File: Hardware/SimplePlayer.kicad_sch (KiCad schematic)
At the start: 4 parts, among them U1 CS43198, U2 XIAO-ESP32S3, U3 OPA1622, U4 OPA1622

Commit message: Schematic sheets
Added new schematic sheets for each system.
Missing some microcontroller connections.
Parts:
- removed U1: CS43198, Custom_Parts:VQFN-40-1EP_5x5mm_P0.4mm_EP3.5x3.5mm_ThermalVias, symbol Custom_Parts:CS43198
- removed U2: XIAO-ESP32S3, Custom_Parts:XIAO-ESP32S3-SMD, symbol Custom_Parts:XIAO-ESP32S3-SMD
- removed U3, U4: OPA1622, Package_SON:Texas_S-PVSON-N10, symbol Amplifier_Audio:OPA1622
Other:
- added sheet Audio (Audio.kicad_sch)
- added sheet Microcontoller (Microcontroller.kicad_sch)
- added sheet Power (Power.kicad_sch)

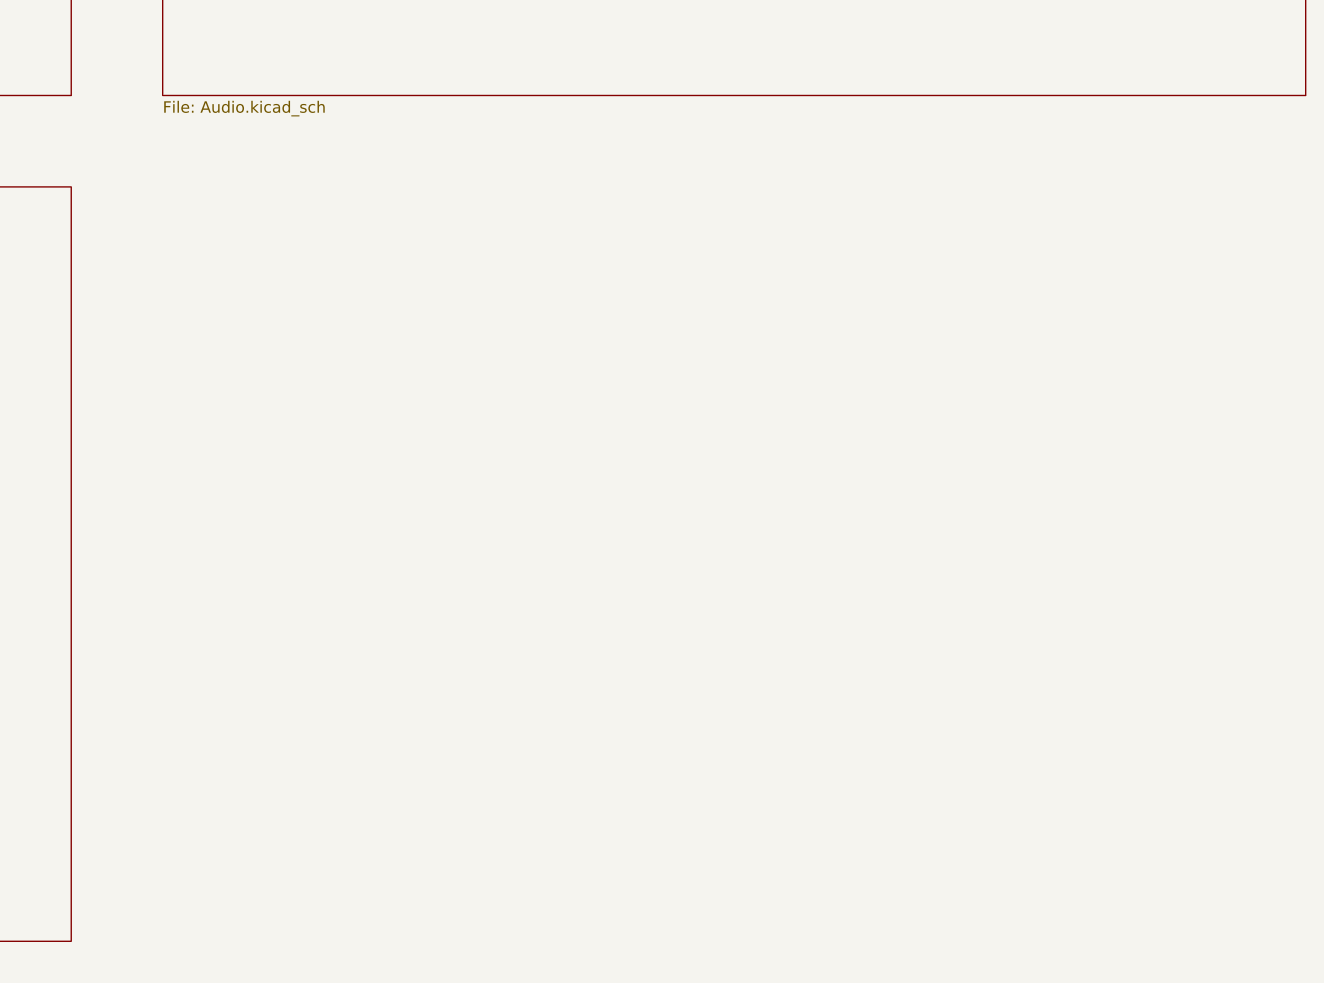
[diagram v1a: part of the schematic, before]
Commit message: Expander and IO
Added an IO expander to the design.
Finished the main connections between the basic components.
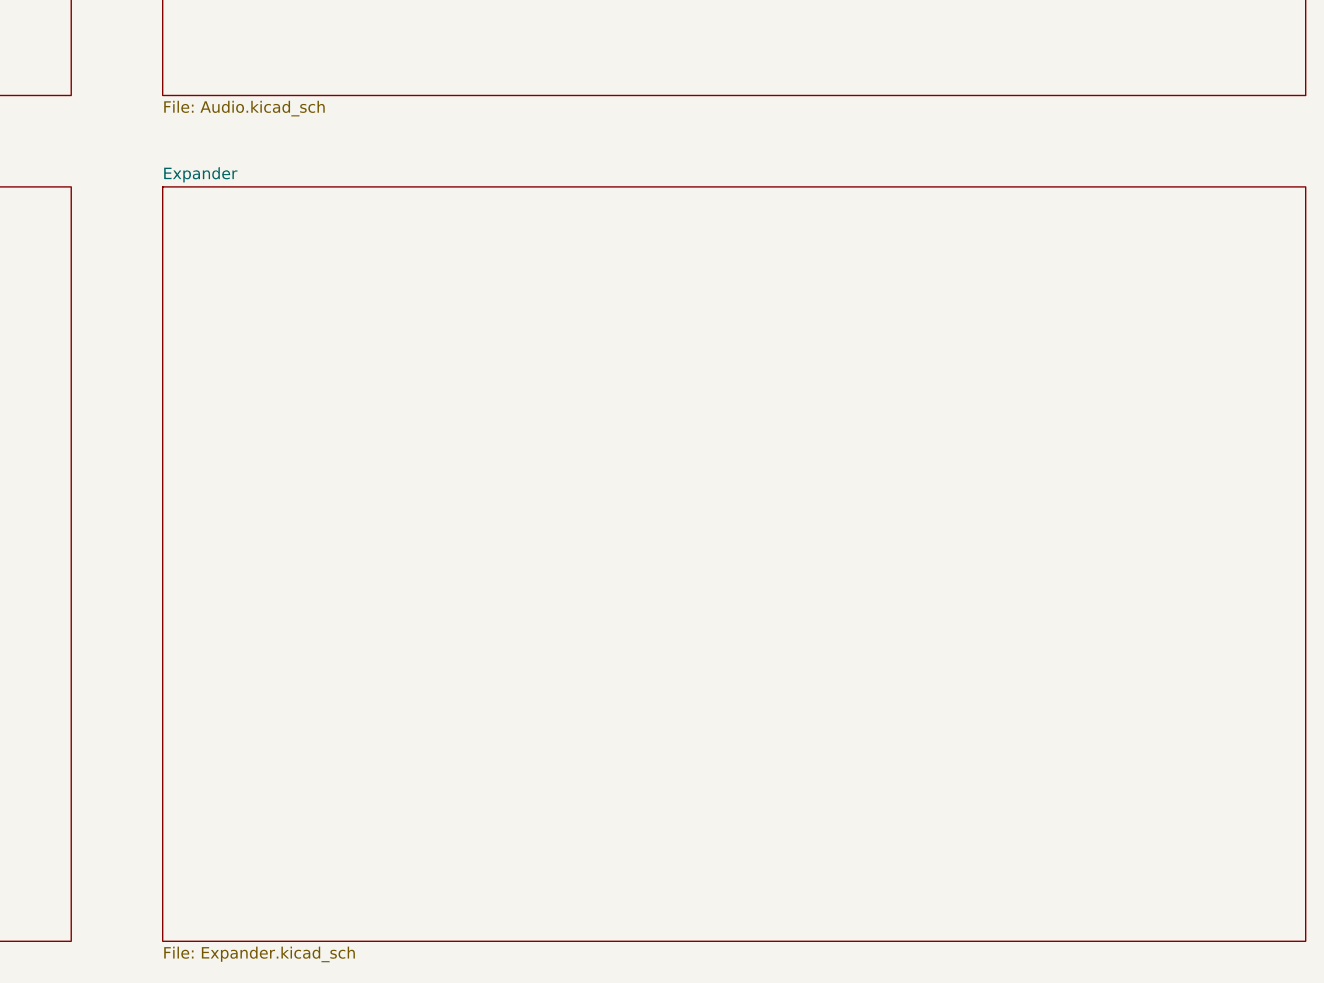
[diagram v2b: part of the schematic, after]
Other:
- added sheet Expander (Expander.kicad_sch)
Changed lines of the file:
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@@
+		)
+	)
+	(sheet
+		(at 210.82 152.4)
+		(size 127 83.82)
+		(exclude_from_sim no)
+		(in_bom yes)
+		(on_board yes)
+		(dnp no)
+		(fields_autoplaced yes)
+		(stroke
+			(width 0.1524)
+			(type solid)
+		)
+		(fill
+			(color 0 0 0 0)
+		)
+		(property "Sheetname" "Expander"
+			(at 210.82 151.6884 0)
+			(show_name no)
+			(do_not_autoplace no)
+			(effects
+				(font
+					(size 1.27 1.27)
+				)
+				(justify left bottom)
+			)
+		)
+		(property "Sheetfile" "Expander.kicad_sch"
+			(at 210.82 236.8046 0)
+			(show_name no)
+			(do_not_autoplace no)
+			(effects
+				(font
+					(size 1.27 1.27)
+				)
+				(justify left top)
+			)
+		)
+		(instances
+			(project "SimplePlayer"
+				(path "/361b87fa-3e7e-4f22-890f-5dc32caef103"
+					(page "5")
+				)
+			)
 		)
 	)
